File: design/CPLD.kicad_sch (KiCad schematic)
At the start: 26 parts, among them IC2 ATF1508AS, J1 JTAG-2x5

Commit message: Sort out R and C types
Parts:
- removed C1, C2, C3, C4, C5, C6, C7, C8: 100nF, Capacitor_SMD:C_0402_1005Metric, symbol Device:C
- removed R1: 1K2, symbol Device:R
- removed R11, R13, R14, R2, R3, R4, R5, R6, R7, R8: 4K7, symbol Device:R
- added C14, C15, C16, C17, C18, C19, C20, C21, C22: 100nF, Capacitor_SMD:C_0805_2012Metric_Pad1.18x1.45mm_HandSolder, symbol Device:C
- added R18, R24, R25, R26, R27, R28, R29, R30: 4K7, Resistor_SMD:R_0805_2012Metric_Pad1.20x1.40mm_HandSolder, symbol Device:R
- added R22, R23: 1K, Resistor_SMD:R_0805_2012Metric_Pad1.20x1.40mm_HandSolder, symbol Device:R
- added R31: 1K2, Resistor_SMD:R_0805_2012Metric_Pad1.20x1.40mm_HandSolder, symbol Device:R
- added Y2: CXO_5032 3.6864MHz, Crystal:Crystal_SMD_5032-4Pin_5.0x3.2mm, symbol Oscillator:CXO_DIP8
- LED1, LED2: footprint (none) -> LED_SMD:LED_0805_2012Metric_Pad1.15x1.40mm_HandSolder
- R10, R9: value 1K -> 4K7; footprint (none) -> Resistor_SMD:R_0805_2012Metric_Pad1.20x1.40mm_HandSolder; LCSC C17512 -> C17515; Mouser ERJ-6ENF1001V -> ERJ-6ENF4701V
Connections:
- net BERR: now also R24.2
- net BGACK: now also R28.2
- net BR: now also R18.2
- net DTACK: now also R31.2
- net GND: now also J1.10 (Pin_10), J1.2 (Pin_2), C14.2, C15.2, C16.2, C17.2, C18.2, C19.2, C20.2, C21.2, C22.2, Y2.4 (GND)
- net HALT: now also R29.2
- net IRQ2: now also R27.2
- net IRQ3: now also R9.2
- net IRQ5: now also R10.2
- net IRQ6: now also R25.2
- net LGEXP: now also R26.2
- net RESET: now also R30.2
- net UART_CLK: now also Y2.5 (OUT)
- net VCC: now also J1.4 (Pin_4), C14.1, C15.1, C16.1, C17.1, C18.1, C19.1, C20.1, C21.1, C22.1, R18.1, R22.1, R23.1, R24.1, R25.1, R26.1, R27.1, R28.1, R29.1, R30.1, R31.1, Y2.1 (EN), Y2.8 (Vcc)
- net at LED2.2 (A): now also R22.2; no longer R10.2
- net at LED1.2 (A): now also R23.2; no longer R9.2
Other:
- moved on the sheet: J1, JP2

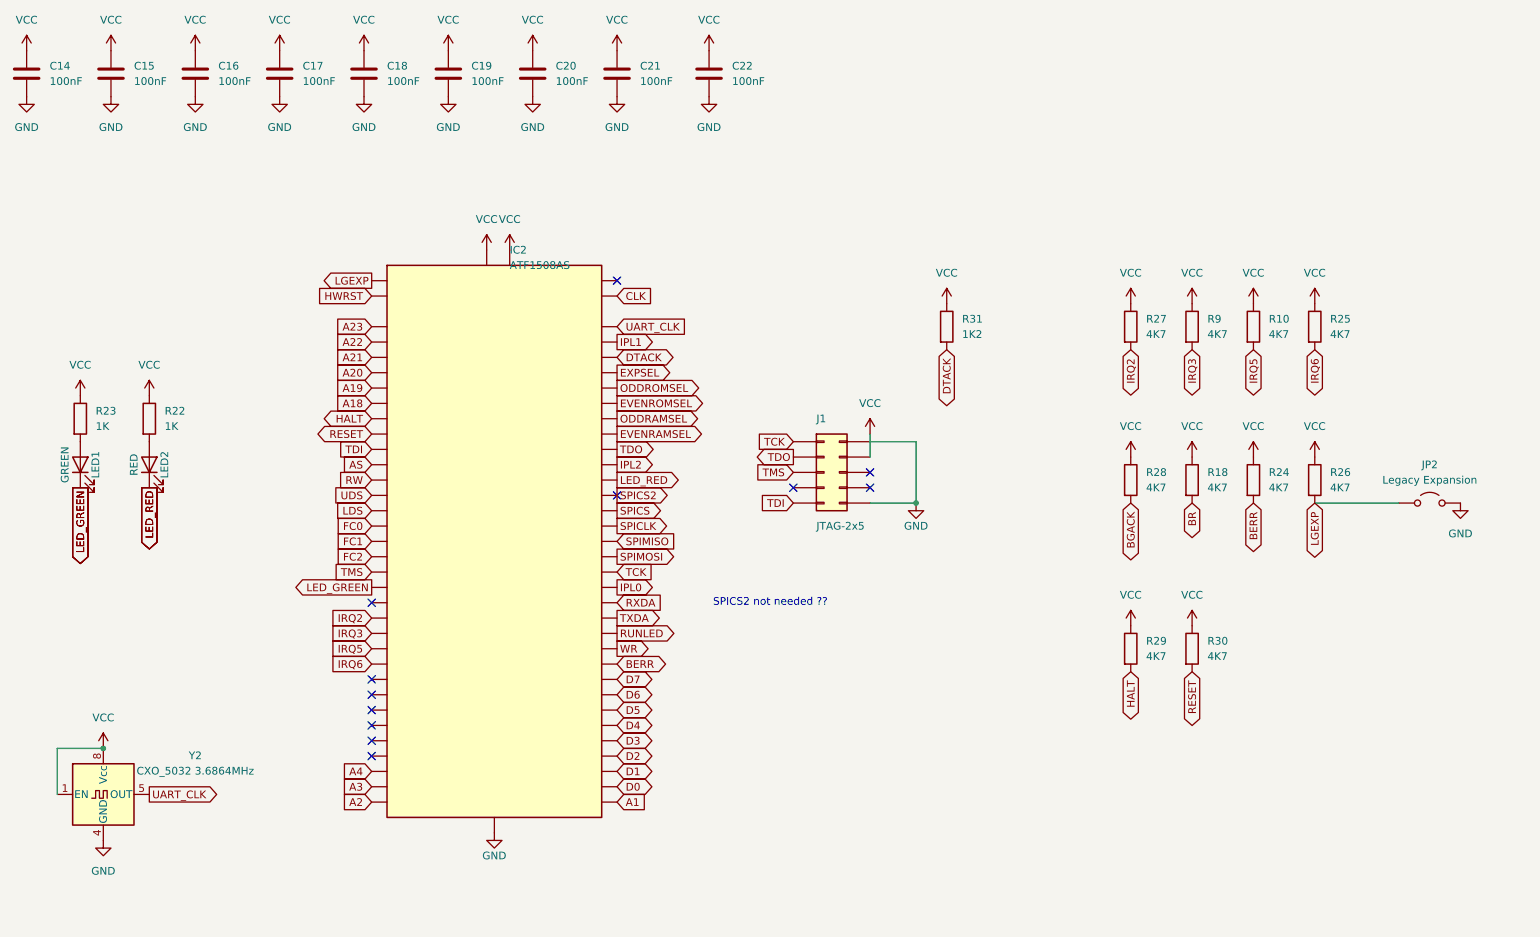
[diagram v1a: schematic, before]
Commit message: Clean ERCC on schmatic
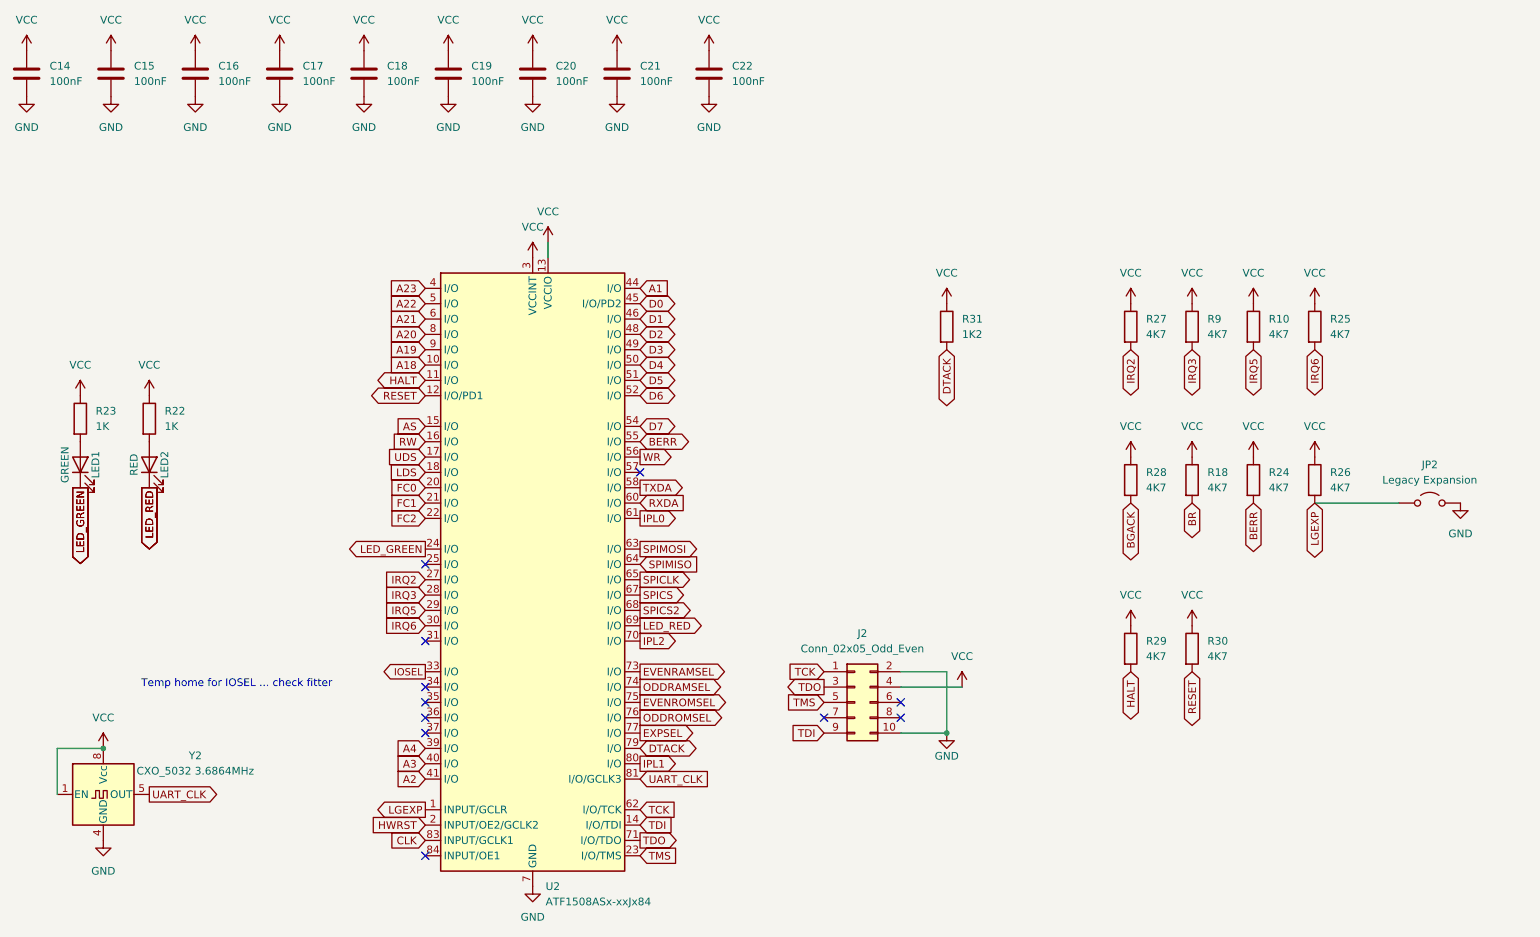
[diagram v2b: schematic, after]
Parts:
- removed IC2: ATF1508AS, Package_LCC:PLCC-84_THT-Socket, symbol rosco_m68k:ATF1508AS-PLCC84
- removed J1: JTAG-2x5, Connector_IDC:IDC-Header_2x05_P2.54mm_Vertical, symbol Connector_Generic:Conn_02x05_Odd_Even
- added J2: Conn_02x05_Odd_Even, symbol Connector_Generic:Conn_02x05_Odd_Even
- added U2: ATF1508ASx-xxJx84, Package_LCC:PLCC-84_29.3x29.3mm_P1.27mm, symbol CPLD_Microchip:ATF1508ASx-xxJx84
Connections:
- net A1: now also U2.44 (I/O)
- net A18: now also U2.10 (I/O)
- net A19: now also U2.9 (I/O)
- net A2: now also U2.41 (I/O)
- net A20: now also U2.8 (I/O)
- net A21: now also U2.6 (I/O)
- net A22: now also U2.5 (I/O)
- net A23: now also U2.4 (I/O)
- net A3: now also U2.40 (I/O)
- net A4: now also U2.39 (I/O)
- net AS: now also U2.15 (I/O)
- net BERR: now also U2.55 (I/O)
- net CLK: now also U2.83 (INPUT/GCLK1)
- net D0: now also U2.45 (I/O/PD2)
- net D1: now also U2.46 (I/O)
- net D2: now also U2.48 (I/O)
- net D3: now also U2.49 (I/O)
- net D4: now also U2.50 (I/O)
- net D5: now also U2.51 (I/O)
- net D6: now also U2.52 (I/O)
- net D7: now also U2.54 (I/O)
- net DTACK: now also U2.79 (I/O)
- net EVENRAMSEL: now also U2.73 (I/O)
- net EVENROMSEL: now also U2.75 (I/O)
- net EXPSEL: now also U2.77 (I/O)
- net FC0: now also U2.20 (I/O)
- net FC1: now also U2.21 (I/O)
- net FC2: now also U2.22 (I/O)
- net GND: now also J2.10 (Pin_10), J2.2 (Pin_2), U2.19 (GND), U2.32 (GND), U2.42 (GND), U2.47 (GND), U2.59 (GND), U2.7 (GND), U2.72 (GND), U2.82 (GND)
- net HALT: now also U2.11 (I/O)
- net HWRST: now also U2.2 (INPUT/OE2/GCLK2)
- net IPL0: now also U2.61 (I/O)
- net IPL1: now also U2.80 (I/O)
- net IPL2: now also U2.70 (I/O)
- net IRQ2: now also U2.27 (I/O)
- net IRQ3: now also U2.28 (I/O)
- net IRQ5: now also U2.29 (I/O)
- net IRQ6: now also U2.30 (I/O)
- net LDS: now also U2.18 (I/O)
- net LED_GREEN: now also U2.24 (I/O)
- net LED_RED: now also U2.69 (I/O)
- net LGEXP: now also U2.1 (INPUT/GCLR)
- net ODDRAMSEL: now also U2.74 (I/O)
- net ODDROMSEL: now also U2.76 (I/O)
- net RESET: now also U2.12 (I/O/PD1)
- net RW: now also U2.16 (I/O)
- net RXDA: now also U2.60 (I/O)
- net SPICLK: now also U2.65 (I/O)
- net SPICS: now also U2.67 (I/O)
- net SPICS2: now also U2.68 (I/O)
- net SPIMISO: now also U2.64 (I/O)
- net SPIMOSI: now also U2.63 (I/O)
- net TCK: now also J2.1 (Pin_1), U2.62 (I/O/TCK)
- net TDI: now also J2.9 (Pin_9), U2.14 (I/O/TDI)
- net TDO: now also J2.3 (Pin_3), U2.71 (I/O/TDO)
- net TMS: now also J2.5 (Pin_5), U2.23 (I/O/TMS)
- net TXDA: now also U2.58 (I/O)
- net UART_CLK: now also U2.81 (I/O/GCLK3)
- net UDS: now also U2.17 (I/O)
- net VCC: now also J2.4 (Pin_4), U2.13 (VCCIO), U2.26 (VCCIO), U2.3 (VCCINT), U2.38 (VCCIO), U2.43 (VCCINT), U2.53 (VCCIO), U2.66 (VCCIO), U2.78 (VCCIO)
- net WR: now also U2.56 (I/O)
- new net IOSEL: U2.33 (I/O)
- no-connect marks 12 -> 11
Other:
- note added: "Temp home for IOSEL ... check fitter"
- note removed: "SPICS2 not needed ??"

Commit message: Further improvements on CPLD pin placement to improve routing
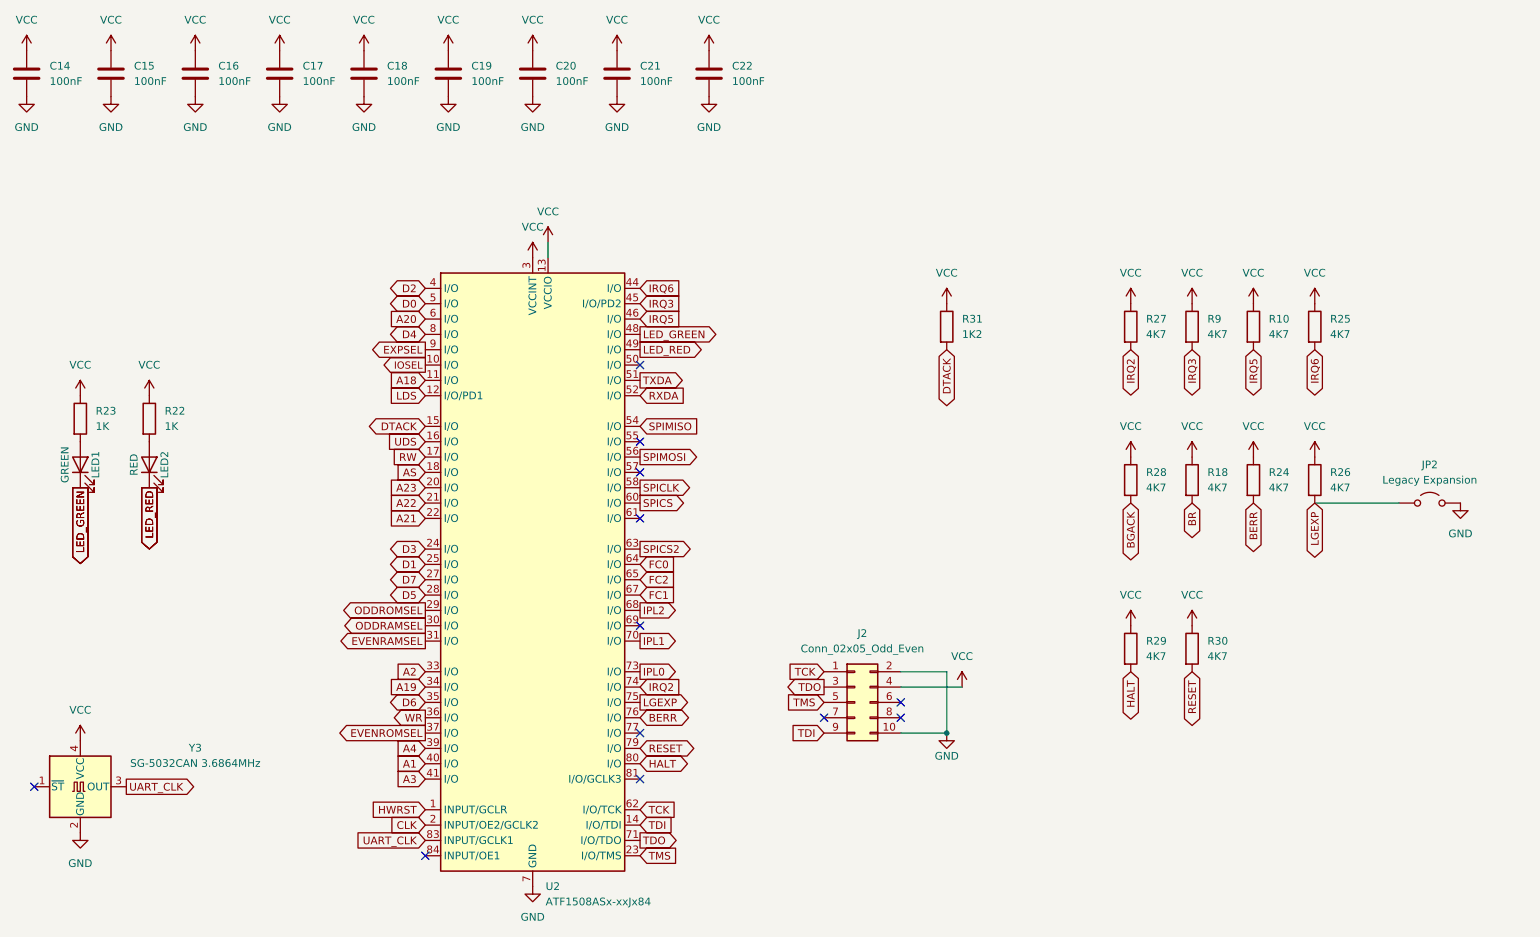
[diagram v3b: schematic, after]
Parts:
- removed Y2: CXO_5032 3.6864MHz, Crystal:Crystal_SMD_5032-4Pin_5.0x3.2mm, symbol Oscillator:CXO_DIP8
- added Y3: SG-5032CAN 3.6864MHz, Oscillator:Oscillator_SMD_SeikoEpson_SG8002LB-4Pin_5.0x3.2mm_HandSoldering, symbol Oscillator:SG-5032CAN
- J2: footprint (none) -> Connector_PinHeader_2.54mm:PinHeader_2x05_P2.54mm_Vertical
- JP2: footprint (none) -> Connector_PinHeader_2.54mm:PinHeader_1x02_P2.54mm_Vertical
- U2: footprint Package_LCC:PLCC-84_29.3x29.3mm_P1.27mm -> Package_LCC:PLCC-84_THT-Socket
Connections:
- net A1: now also U2.40 (I/O); no longer U2.44 (I/O)
- net A18: now also U2.11 (I/O); no longer U2.10 (I/O)
- net A19: now also U2.34 (I/O); no longer U2.9 (I/O)
- net A2: now also U2.33 (I/O); no longer U2.41 (I/O)
- net A20: now also U2.6 (I/O); no longer U2.8 (I/O)
- net A21: now also U2.22 (I/O); no longer U2.6 (I/O)
- net A22: now also U2.21 (I/O); no longer U2.5 (I/O)
- net A23: now also U2.20 (I/O); no longer U2.4 (I/O)
- net A3: now also U2.41 (I/O); no longer U2.40 (I/O)
- net AS: now also U2.18 (I/O); no longer U2.15 (I/O)
- net BERR: now also U2.76 (I/O); no longer U2.55 (I/O)
- net CLK: now also U2.2 (INPUT/OE2/GCLK2); no longer U2.83 (INPUT/GCLK1)
- net D0: now also U2.5 (I/O); no longer U2.45 (I/O/PD2)
- net D1: now also U2.25 (I/O); no longer U2.46 (I/O)
- net D2: now also U2.4 (I/O); no longer U2.48 (I/O)
- net D3: now also U2.24 (I/O); no longer U2.49 (I/O)
- net D4: now also U2.8 (I/O); no longer U2.50 (I/O)
- net D5: now also U2.28 (I/O); no longer U2.51 (I/O)
- net D6: now also U2.35 (I/O); no longer U2.52 (I/O)
- net D7: now also U2.27 (I/O); no longer U2.54 (I/O)
- net DTACK: now also U2.15 (I/O); no longer U2.79 (I/O)
- net EVENRAMSEL: now also U2.31 (I/O); no longer U2.73 (I/O)
- net EVENROMSEL: now also U2.37 (I/O); no longer U2.75 (I/O)
- net EXPSEL: now also U2.9 (I/O); no longer U2.77 (I/O)
- net FC0: now also U2.64 (I/O); no longer U2.20 (I/O)
- net FC1: now also U2.67 (I/O); no longer U2.21 (I/O)
- net FC2: now also U2.65 (I/O); no longer U2.22 (I/O)
- net GND: now also Y3.2 (GND)
- net HALT: now also U2.80 (I/O); no longer U2.11 (I/O)
- net HWRST: now also U2.1 (INPUT/GCLR); no longer U2.2 (INPUT/OE2/GCLK2)
- net IOSEL: now also U2.10 (I/O); no longer U2.33 (I/O)
- net IPL0: now also U2.73 (I/O); no longer U2.61 (I/O)
- net IPL1: now also U2.70 (I/O); no longer U2.80 (I/O)
- net IPL2: now also U2.68 (I/O); no longer U2.70 (I/O)
- net IRQ2: now also U2.74 (I/O); no longer U2.27 (I/O)
- net IRQ3: now also U2.45 (I/O/PD2); no longer U2.28 (I/O)
- net IRQ5: now also U2.46 (I/O); no longer U2.29 (I/O)
- net IRQ6: now also U2.44 (I/O); no longer U2.30 (I/O)
- net LDS: now also U2.12 (I/O/PD1); no longer U2.18 (I/O)
- net LED_GREEN: now also U2.48 (I/O); no longer U2.24 (I/O)
- net LED_RED: now also U2.49 (I/O); no longer U2.69 (I/O)
- net LGEXP: now also U2.75 (I/O); no longer U2.1 (INPUT/GCLR)
- net ODDRAMSEL: now also U2.30 (I/O); no longer U2.74 (I/O)
- net ODDROMSEL: now also U2.29 (I/O); no longer U2.76 (I/O)
- net RESET: now also U2.79 (I/O); no longer U2.12 (I/O/PD1)
- net RW: now also U2.17 (I/O); no longer U2.16 (I/O)
- net RXDA: now also U2.52 (I/O); no longer U2.60 (I/O)
- net SPICLK: now also U2.58 (I/O); no longer U2.65 (I/O)
- net SPICS: now also U2.60 (I/O); no longer U2.67 (I/O)
- net SPICS2: now also U2.63 (I/O); no longer U2.68 (I/O)
- net SPIMISO: now also U2.54 (I/O); no longer U2.64 (I/O)
- net SPIMOSI: now also U2.56 (I/O); no longer U2.63 (I/O)
- net TXDA: now also U2.51 (I/O); no longer U2.58 (I/O)
- net UART_CLK: now also U2.83 (INPUT/GCLK1), Y3.3 (OUT); no longer U2.81 (I/O/GCLK3)
- net UDS: now also U2.16 (I/O); no longer U2.17 (I/O)
- net VCC: now also Y3.4 (VCC)
- net WR: now also U2.36 (I/O); no longer U2.56 (I/O)
- no-connect marks 11 -> 12
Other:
- note removed: "Temp home for IOSEL ... check fitter"
